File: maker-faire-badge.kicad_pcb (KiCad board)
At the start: 2 copper layers, 82.6 x 31.8 mm, 47 parts, among them J1 USB-C, Q1 2N3906, Q2 2N3906, Q3 2N3906, Q4 2N3906, Q5 2N3906, Q6 2N3906

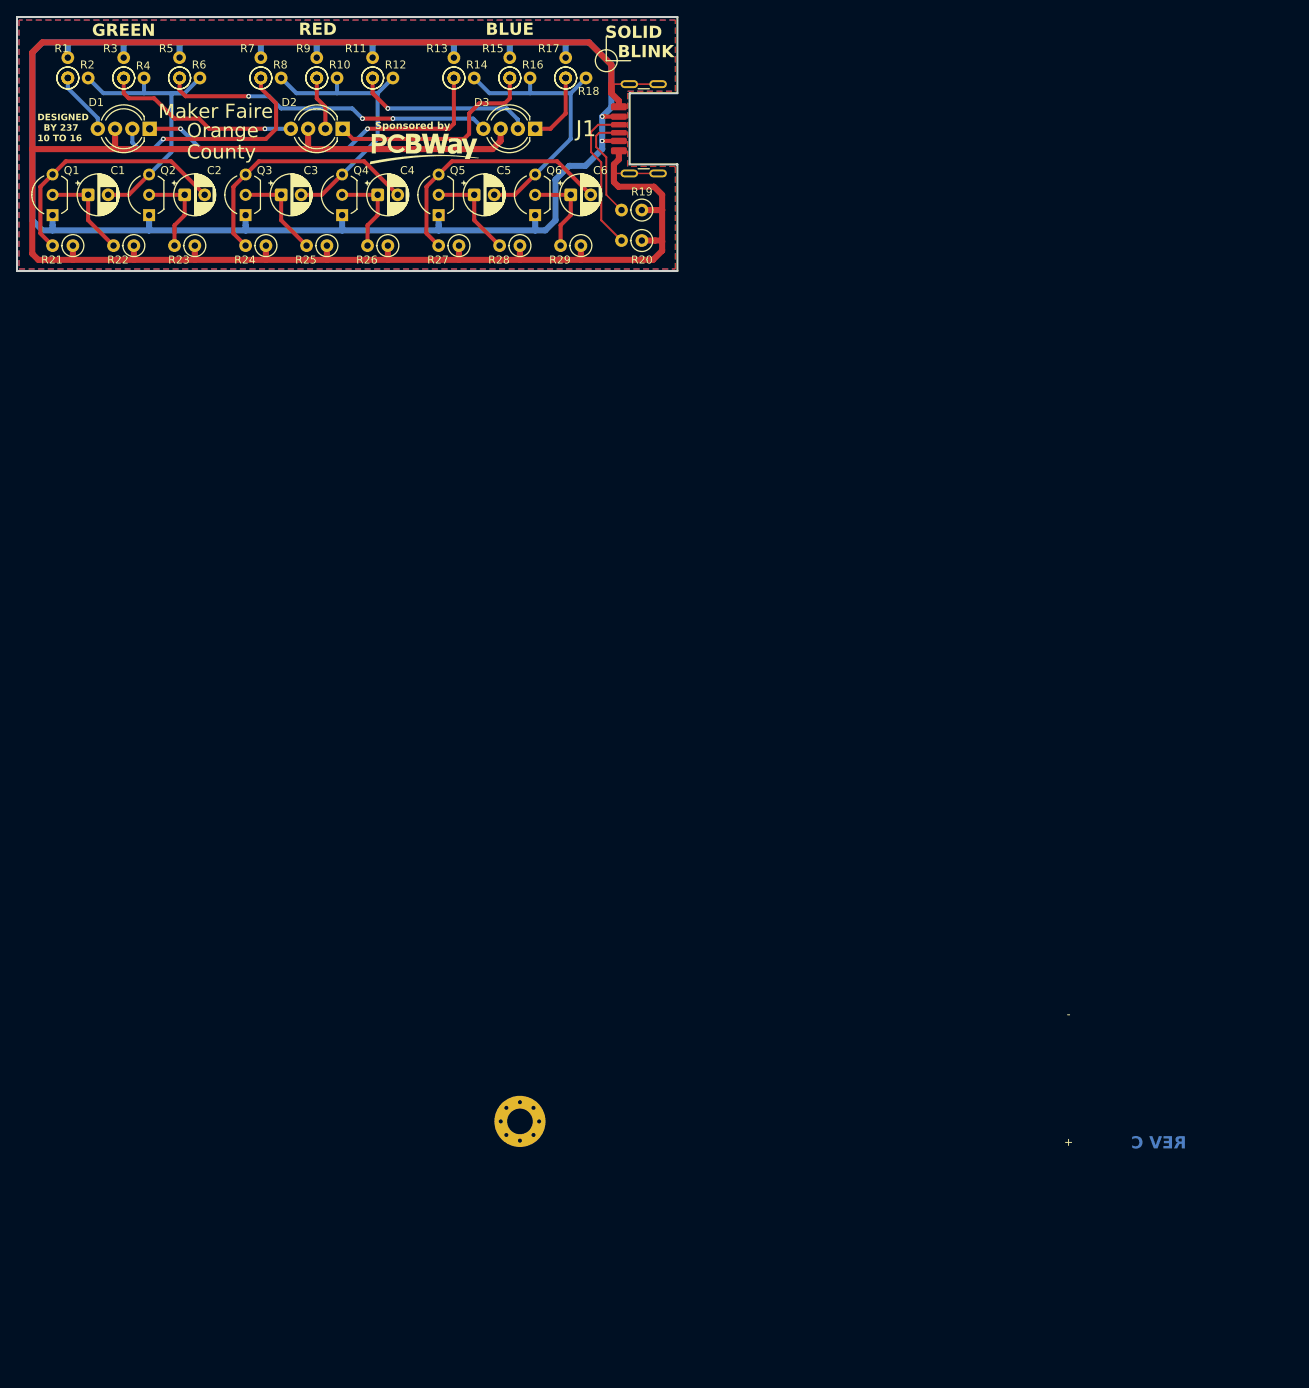
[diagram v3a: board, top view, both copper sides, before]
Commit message: BOM and Fabrication Note corrections
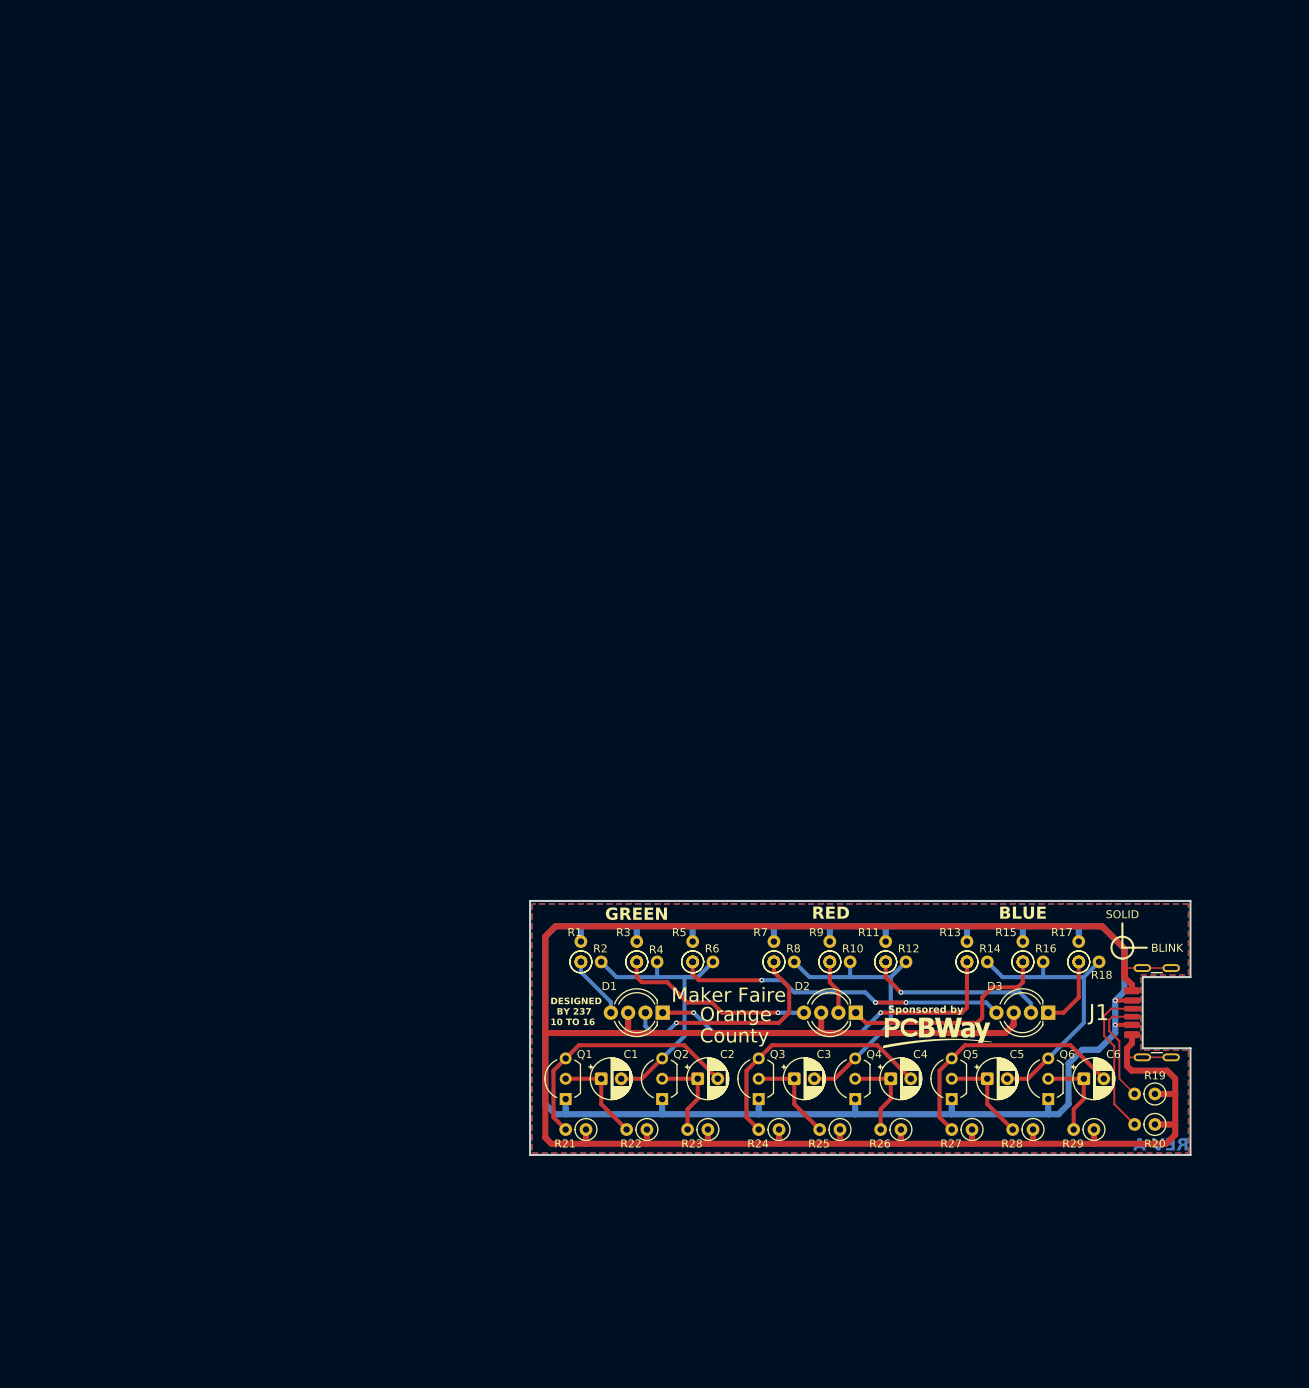
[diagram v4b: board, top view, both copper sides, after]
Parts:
- removed H1: MountingHole_Pad, MountingHole:MountingHole_3.2mm_M3_Pad_Via
- R1, R13, R15, R3: value 205 -> 82
- R10, R12, R8: value 95.3 -> 150
- R11, R7, R9: value 205 -> 150
- R14, R16, R2, R4: value 95.3 -> 82
- R17, R5: value 133 -> 82
- R18, R6: value 24.9 -> 82
- R21, R24, R27: value 261 -> 270
- moved R11 127.8 mm to (149.9, 63.5)
- moved R12 127.8 mm to (149.9, 63.5)
- moved D2 127.8 mm to (146.1, 69.8)
- moved D3 127.8 mm to (170.2, 69.8)
- moved Q1 127.8 mm to (109.9, 80.6)
- moved Q2 127.8 mm to (121.9, 80.6)
- moved Q3 127.8 mm to (134.0, 80.6)
- moved Q4 127.8 mm to (146.1, 80.6)
- moved Q5 127.8 mm to (158.1, 80.6)
- moved Q6 127.8 mm to (170.2, 80.6)
- moved R23 127.8 mm to (127.6, 84.5)
- moved R24 127.8 mm to (136.5, 84.5)
- moved R25 127.8 mm to (144.1, 84.5)
- moved R27 127.8 mm to (160.7, 84.5)
- moved R28 127.8 mm to (168.3, 84.5)
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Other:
- board size 82.6 x 31.8 mm -> 82.6 x 31.7 mm
- board text added: "REV A"
- board text removed: "+"
- board text removed: "-"
- board text removed: "BLINK LED 1"
- board text removed: "BLINK LED 2"
- board text removed: "BLINK LED 3"
- board text removed: "K"
- board text removed: "LED SOLID BLINK 1 R15 R8 2 R14 R7 3 R16 R9"
- board text removed: "LEDS 1,2,3 SOLID/BLINK"
- board text removed: "Maker Faire '25 Orange County"
- board text removed: "REMOVE BATTERY BEFORE CONNECTING THE USB"
- board text removed: "REV B"
- board text removed: "REV C"
- board text removed: "Space for Manufacturer Markings on bottom side of board"
- board text removed: "THE BATTERY OVERRIDES USB POWER"
